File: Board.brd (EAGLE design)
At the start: 115.7 x 77.4 mm, 56 parts, among them IC2 LM358N, Q1 IRF3205, Q2 IRF3205, Q3 IRF3205, Q4 IRF3205, Q5 IRF3205, Q6 IRF3205, Q7 IRF3205, Q8 IRF3205, X1 12Vcc IN, X2 MOTOR DC, X3 Resistencia Shunt

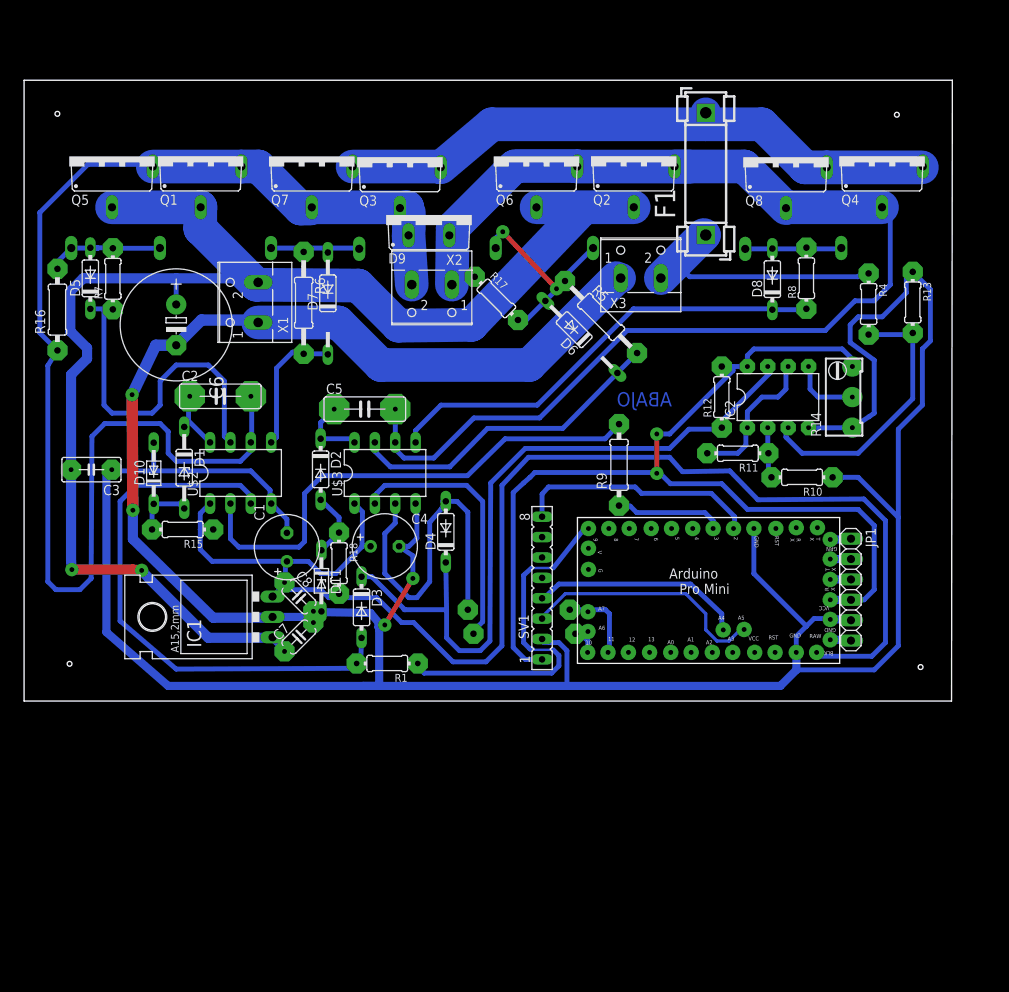
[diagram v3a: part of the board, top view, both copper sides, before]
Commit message: Ver 5
Board: The power consumption is huge, so i needed to make thicker the board contacts. I also included a battery charge sensing.
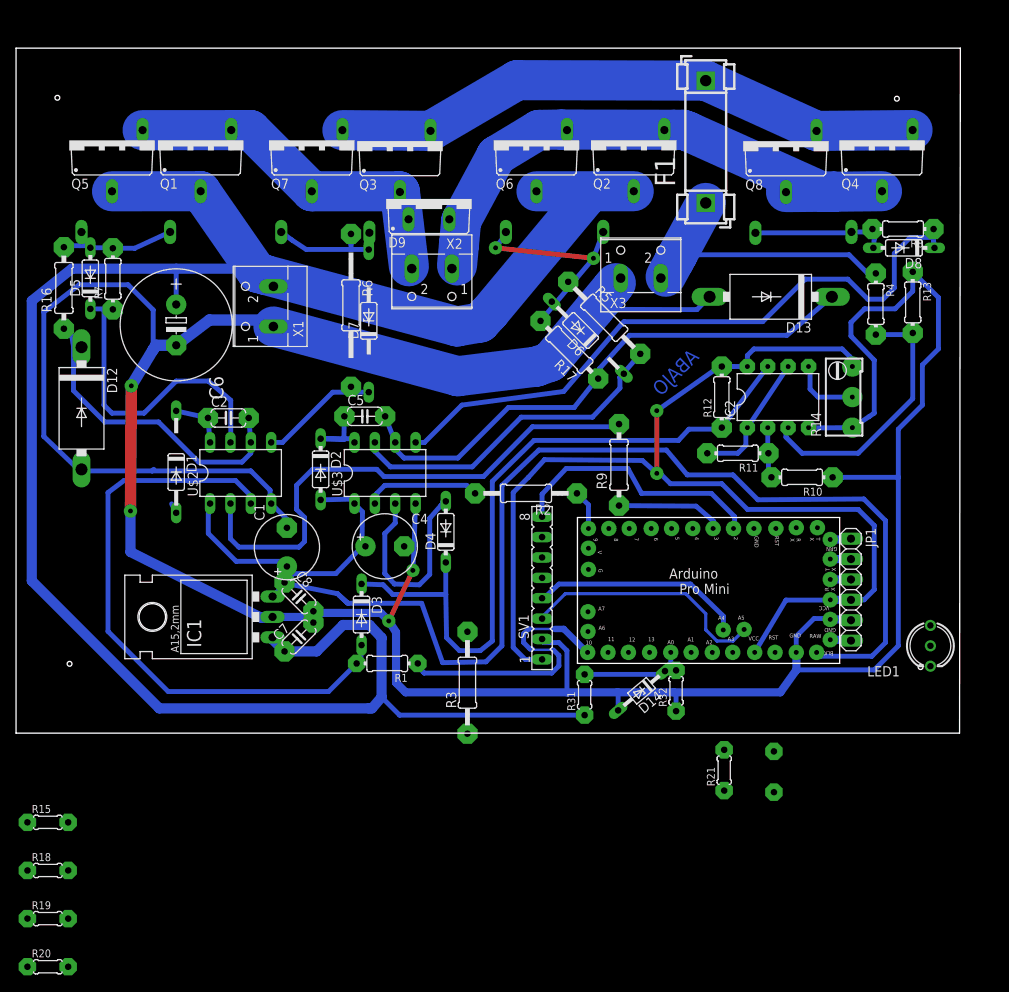
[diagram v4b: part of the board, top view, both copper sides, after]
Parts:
- removed C3: (no value), rcl:C050-030X075
- removed D10, D11: (no value), diode Victor:DO34Z7
- added D12, D13: 1N5400, diode Victor:DO201-15
- added D14: 5.1V, diode Victor:DO34Z7
- added LED1: L-59EGW-CA, led:L-59EGW-CA
- added R19, R20: 47k, rcl:0204/5
- added R21, R22: 470, rcl:0204/5
- added R31, R32: (no value), rcl:0204/5
- C1, C4: value 4.7uF -> 10uF
- C2, C5: value 470nF -> 220nF; device rcl:C075-032X103 -> rcl:C050-024X044
- C6: value (none) -> 2200uF 35V
- D1: value 1N821 -> 1n4148; device diode:DO35Z10 -> diode:DO35-10
- D2, D3, D4: value 1N4148DO35-7 -> 1n4148
- D5, D8: value 1N4148DO35-7 -> 1N4148
- D6: value 1N4446 -> 1N4148
- D7: value 1N4148DO35-10 -> 1N4148; device diode:DO35-10 -> diode:DO35Z10
- D9: value BR210 -> 1k5
- IC1: value (none) -> 7812
- R10, R11, R13, R14, R4: value (none) -> 10k
- R12: value (none) -> 1k
- R15, R18: value (none) -> 47k; device rcl_Victor:0204/7 -> rcl:0204/5
- R16: value 1k -> 1k (NO SE)
- R17: value 1k -> 1k (NO SE); device rcl_Victor:0204/7 -> rcl_Victor:0207/10
- R5, R7, R8: value 10 -> 6k8
- R6: value 10 -> 6k8; device rcl_Victor:0207/12 -> rcl_Victor:0207/15
- moved R18 52.8 mm to (-17.0, 35.0), turned to 0 degrees
- moved R15 40.2 mm to (-17.0, 41.0), turned to 0 degrees
- moved R2 17.5 mm to (42.6, 82.0), flipped to the top, turned to 180 degrees
- moved D8 16.9 mm to (89.7, 112.6), turned to 180 degrees
- moved R8 13.5 mm to (89.6, 114.9), turned to 180 degrees
- moved R3 11.1 mm to (35.3, 58.4), flipped to the top, turned to 90 degrees
- moved R17 11.1 mm to (48.0, 99.9), turned to 135 degrees
- moved R6 5.91 mm to (20.8, 105.4)
- moved D7 5.18 mm to (23.0, 103.5)
- moved F1 4.00 mm to (65.0, 118.2)
- moved C2 2.88 mm to (5.50, 91.4)
- moved R16 2.82 mm to (-15.0, 107.6)
- moved D1 2.24 mm to (-1.00, 87.2)
- moved D9 2.00 mm to (30.5, 118.7)
- moved Q1 2.00 mm to (2.05, 126.0)
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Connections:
- new net N$30: LED1.3, R21.1
- new net N$34: C5.2, D13.C, D9.T2, Q2.S, Q4.D, Q6.S, Q8.D, R17.1, U$3.6, X2.1
- new net N$61: D14.C, R31.2, R32.2, U$1.A0
- net +12V: now also D1.A, D2.A; no longer R15.1, R18.2
- net +24V: now also R31.1; no longer C3.2
- net +5V: now also U$1.VCC
- net GND: now also D12.A, D13.A, D14.A, LED1.2, R15.2, R18.1, R19.2, R20.2, R32.1; no longer C3.1, D10.A, D11.A
- net N$13: now also D12.C
- net N$16: now also LED1.1, R22.1; no longer C5.2, D9.T2, Q2.S, Q4.D, Q6.S, Q8.D, R17.1, U$3.6, X2.1
- net N$17: now also R21.2, U$1.6; no longer D1.A, D10.C, R15.2
- net N$19: now also R22.2, U$1.5; no longer R2.1, U$1.10
- net N$29: now also R2.1, R20.1, U$1.9; no longer D11.C, D2.A, R18.1
- net N$33: now also R15.1
- net N$7: now also R19.1, U$1.10; no longer U$1.9
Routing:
- net N$16: track 165.7 -> 0.00 mm
- net N$34: track 0.00 -> 149.1 mm
- net +24V: track 183.0 -> 268.2 mm, vias 2 -> 0
- net N$13: track 165.5 -> 91.5 mm
- net N$25: track 56.6 -> 81.9 mm
- net N$5: track 33.4 -> 14.4 mm
- net N$6: track 44.0 -> 26.3 mm
- net GND: track 443.9 -> 426.8 mm
- net +5V: track 124.2 -> 139.5 mm
- net N$61: track 0.00 -> 14.3 mm
- net N$33: track 10.1 -> 0.00 mm
- net N$7: track 44.7 -> 35.8 mm
- net N$17: track 7.31 -> 0.00 mm
- net +12V: track 173.1 -> 179.3 mm
- net N$3: track 32.7 -> 38.9 mm
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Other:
- board size 115.7 x 77.4 mm -> 117.7 x 85.4 mm

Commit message: Ver 6
Board: I added some shunt diodes to avoid voltage spikes that could burn out the circuit.
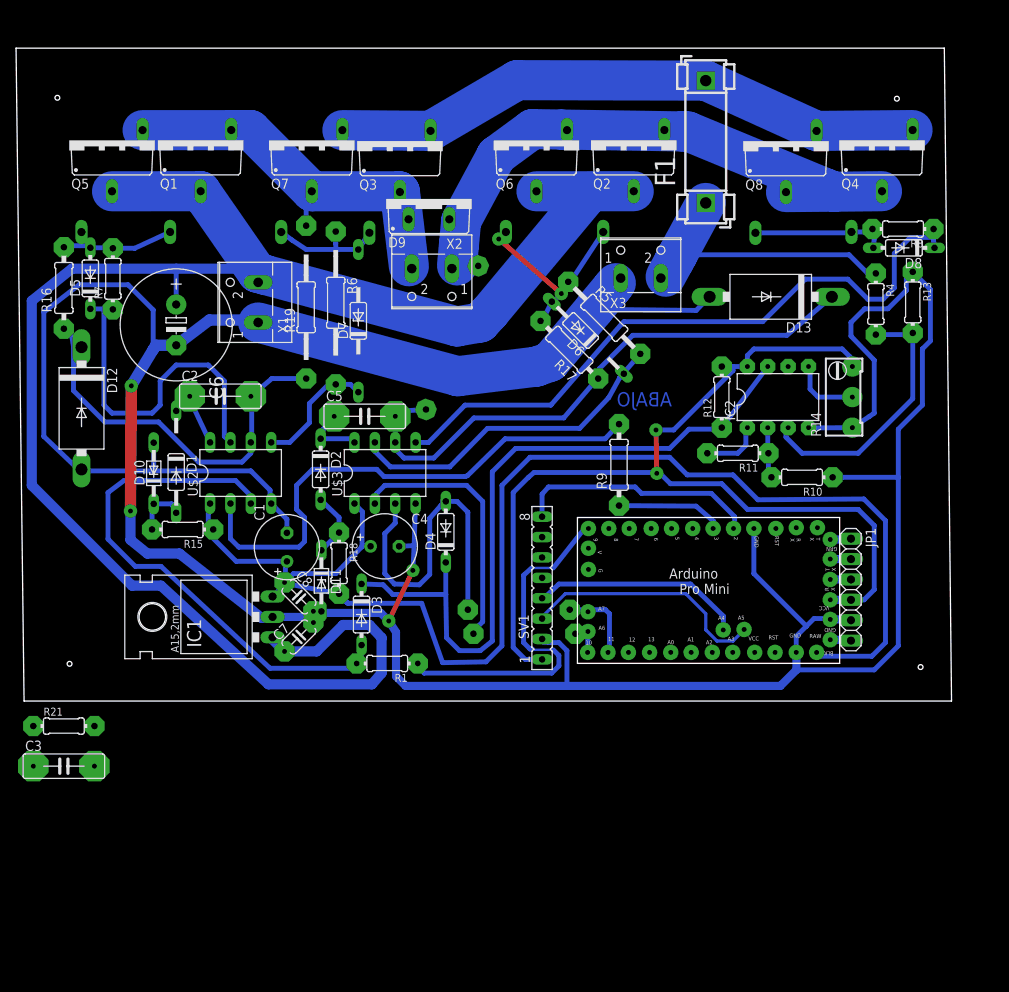
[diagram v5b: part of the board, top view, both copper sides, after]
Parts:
- removed D14: 5.1V, diode Victor:DO34Z7
- removed LED1: L-59EGW-CA, led:L-59EGW-CA
- removed R22: 470, rcl:0204/5
- removed R31, R32: (no value), rcl:0204/5
- added C3: 220nF, rcl:C075-032X103
- added D10, D11: 5.4V, diode Victor:DO34Z7
- C1: value 10uF -> 1uF
- C2, C5: device rcl:C050-024X044 -> rcl:C075-032X103
- C4: value 10uF -> (none)
- D1: value 1n4148 -> 1N4446
- D2, D3, D4: value 1n4148 -> 1N4148DO35-7
- D5, D8: value 1N4148 -> 1N4148DO35-7
- D6: value 1N4148 -> 1N4446
- D7: value 1N4148 -> 1N821
- IC1: value 7812 -> (none)
- R15, R18: value 47k -> (none); device rcl:0204/5 -> rcl_Victor:0204/7
- R16, R17: value 1k (NO SE) -> 1k
- R19, R20: value 47k -> (none); device rcl:0204/5 -> rcl_Victor:0207/15
- R21: value 470 -> 1k; device rcl:0204/5 -> rcl_Victor:0204/7
- moved R20 93.8 mm to (33.6, 102.0), flipped to the bottom, turned to 290 degrees
- moved R19 82.7 mm to (15.2, 105.2), turned to 90 degrees
- moved R21 82.5 mm to (-15.0, 53.0), turned to 0 degrees
- moved R18 52.8 mm to (19.3, 73.3), turned to 270 degrees
- moved R15 40.2 mm to (-0.20, 77.5), turned to 180 degrees
- moved R2 17.5 mm to (42.4, 64.5), flipped to the bottom, turned to 0 degrees
- moved R3 11.1 mm to (41.7, 67.5), flipped to the bottom, turned to 0 degrees
- moved C2 2.88 mm to (4.50, 94.1)
- moved X1 1.96 mm to (7.95, 105.8)
- moved R6 1.92 mm to (18.9, 105.7)
- moved D7 1.30 mm to (21.7, 103.5)
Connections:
- removed net N$30: LED1.3, R21.1
- removed net N$61: D14.C, R31.2, R32.2, U$1.A0
- new net N$35: D9.T1, Q1.S, Q3.D, Q5.S, Q7.D, R19.2, X2.2
- new net N$36: C5.2, D13.C, R17.1, R20.2, U$3.6
- net +12V: now also R15.1, R18.2; no longer D1.A, D2.A
- net +24V: no longer R31.1
- net +5V: no longer U$1.VCC
- net GND: now also C3.2, D10.A, D11.A; no longer D14.A, LED1.2, R15.2, R18.1, R19.2, R20.2, R32.1
- net N$13: now also R19.1; no longer D9.T1, Q1.S, Q3.D, Q5.S, Q7.D, X2.2
- net N$16: now also C3.1, IC2.6, R21.2; no longer LED1.1, R22.1
- net N$17: now also D1.A, D10.C, R15.2; no longer R21.2, U$1.6
- net N$19: now also R2.1, U$1.10; no longer R22.2, U$1.5
- net N$22: now also R21.1; no longer IC2.6
- net N$29: now also D11.C, D2.A, R18.1; no longer R2.1, R20.1, U$1.9
- net N$33: no longer R15.1
- net N$34: now also R20.1; no longer C5.2, D13.C, R17.1, U$3.6
- net N$7: now also U$1.9; no longer R19.1, U$1.10
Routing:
- net N$36: track 0.00 -> 72.3 mm
- net N$34: track 149.1 -> 81.5 mm
- net N$35: track 0.00 -> 54.4 mm
- net +24V: track 268.2 -> 226.5 mm
- net N$13: track 91.5 -> 52.2 mm
- net N$5: track 14.4 -> 33.4 mm
- net N$6: track 26.3 -> 42.1 mm
- net +5V: track 139.5 -> 124.6 mm
- net N$61: track 14.3 -> 0.00 mm
- net GND: track 426.8 -> 437.6 mm
- net N$33: track 0.00 -> 10.1 mm
- net N$22: track 16.7 -> 7.49 mm
- net N$7: track 35.8 -> 44.7 mm
- net N$28: track 75.2 -> 66.6 mm
- net N$17: track 0.00 -> 6.75 mm
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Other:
- board size 117.7 x 85.4 mm -> 116.6 x 81.4 mm

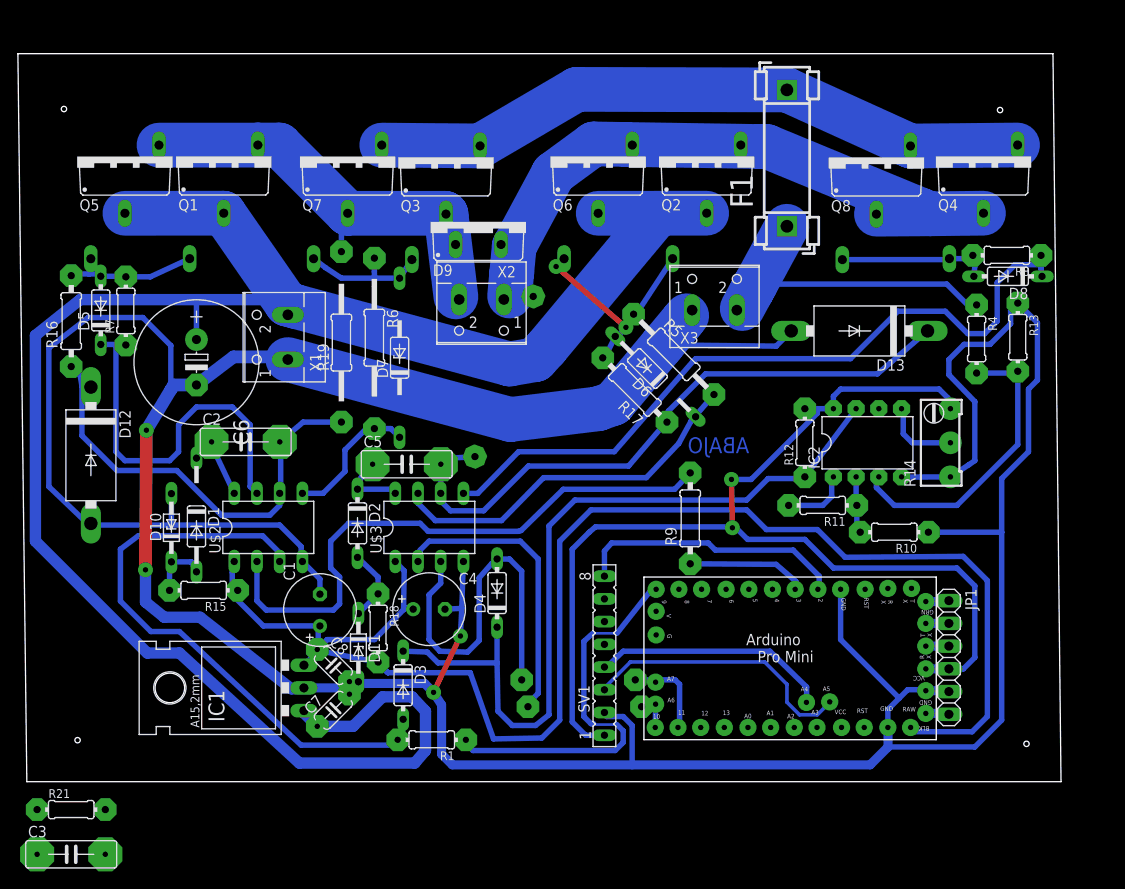
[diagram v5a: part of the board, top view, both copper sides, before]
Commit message: Ver 7
Board: Some mixed improvements:
Algorithm: I needed to invert the X and Y axis.
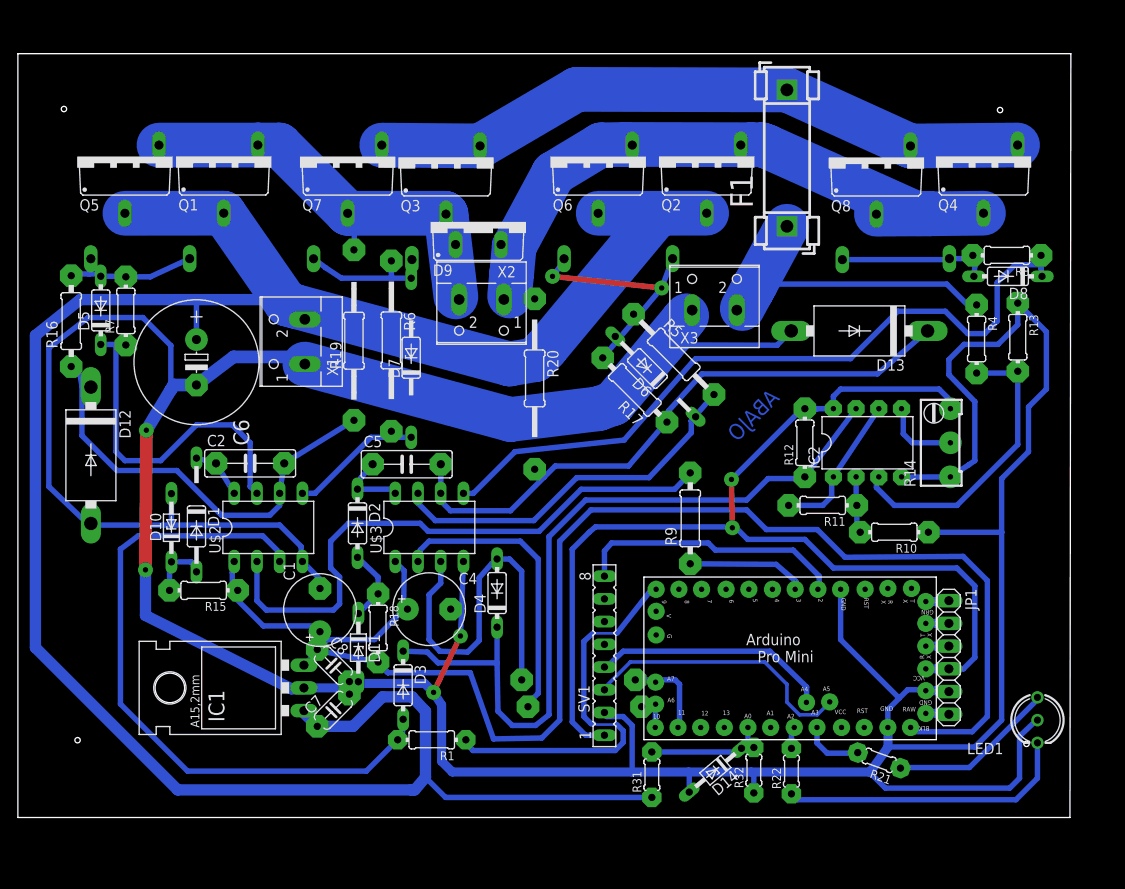
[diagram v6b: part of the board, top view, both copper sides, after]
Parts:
- removed C3: 220nF, rcl:C075-032X103
- added D14: 5.1V, diode Victor:DO34Z7
- added LED1: L-59EGW-CA, led:L-59EGW-CA
- added R22, R31, R32: (no value), rcl:0204/5
- R21: value 1k -> (none); device rcl_Victor:0204/7 -> rcl:0204/5
- moved R21 90.5 mm to (75.3, 58.5), turned to 160 degrees
- moved R20 3.30 mm to (36.8, 101.2), flipped to the top, turned to 270 degrees
- moved C2 2.45 mm to (5.00, 91.7)
- moved X1 1.96 mm to (9.85, 105.3)
- moved R6 1.92 mm to (20.8, 105.4)
- moved R19 1.41 mm to (16.6, 105.4)
- moved D7 1.30 mm to (23.0, 103.5)
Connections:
- new net N$30: LED1.3, R21.1
- new net N$38: R21.2, U$1.A3
- new net N$39: R22.2, U$1.A2
- new net N$61: D14.C, R31.2, R32.2, U$1.A0
- net +24V: now also R31.1
- net GND: now also D14.A, LED1.2, R32.1; no longer C3.2
- net N$16: now also LED1.1, R22.1; no longer C3.1, IC2.6, R21.2
- net N$22: now also IC2.6; no longer R21.1
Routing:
- net +24V: track 226.5 -> 268.2 mm
- net N$16: track 0.00 -> 32.7 mm
- net GND: track 437.6 -> 470.2 mm
- net N$30: track 0.00 -> 18.7 mm
- net N$61: track 0.00 -> 14.3 mm
- net N$22: track 7.49 -> 16.7 mm
- net N$28: track 66.6 -> 75.2 mm
- net N$38: track 0.00 -> 6.79 mm
- net N$23: track 43.2 -> 38.7 mm
- net N$4: track 25.4 -> 29.4 mm
- net N$2: track 8.91 -> 6.18 mm
- net N$36: track 72.3 -> 69.7 mm
- net N$39: track 0.00 -> 2.47 mm
- net N$34: track 81.5 -> 83.9 mm
- net N$13: track 52.2 -> 50.3 mm
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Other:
- board size 116.6 x 81.4 mm -> 117.7 x 85.4 mm
